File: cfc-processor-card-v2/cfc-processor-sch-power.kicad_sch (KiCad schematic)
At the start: 88 parts, among them Q1 DMP2240UDM, Q2 PMV45EN, Q3 DMP3050LVT-7, Q4 DMP3050LVT-7, Q5 PMV45EN, U1 MAX7310ATE+, U2 MIC842LYC5, U3 MIC842LYC5, U4 TS5A21366, U5 MAX4211FETE, U6 TPS62112

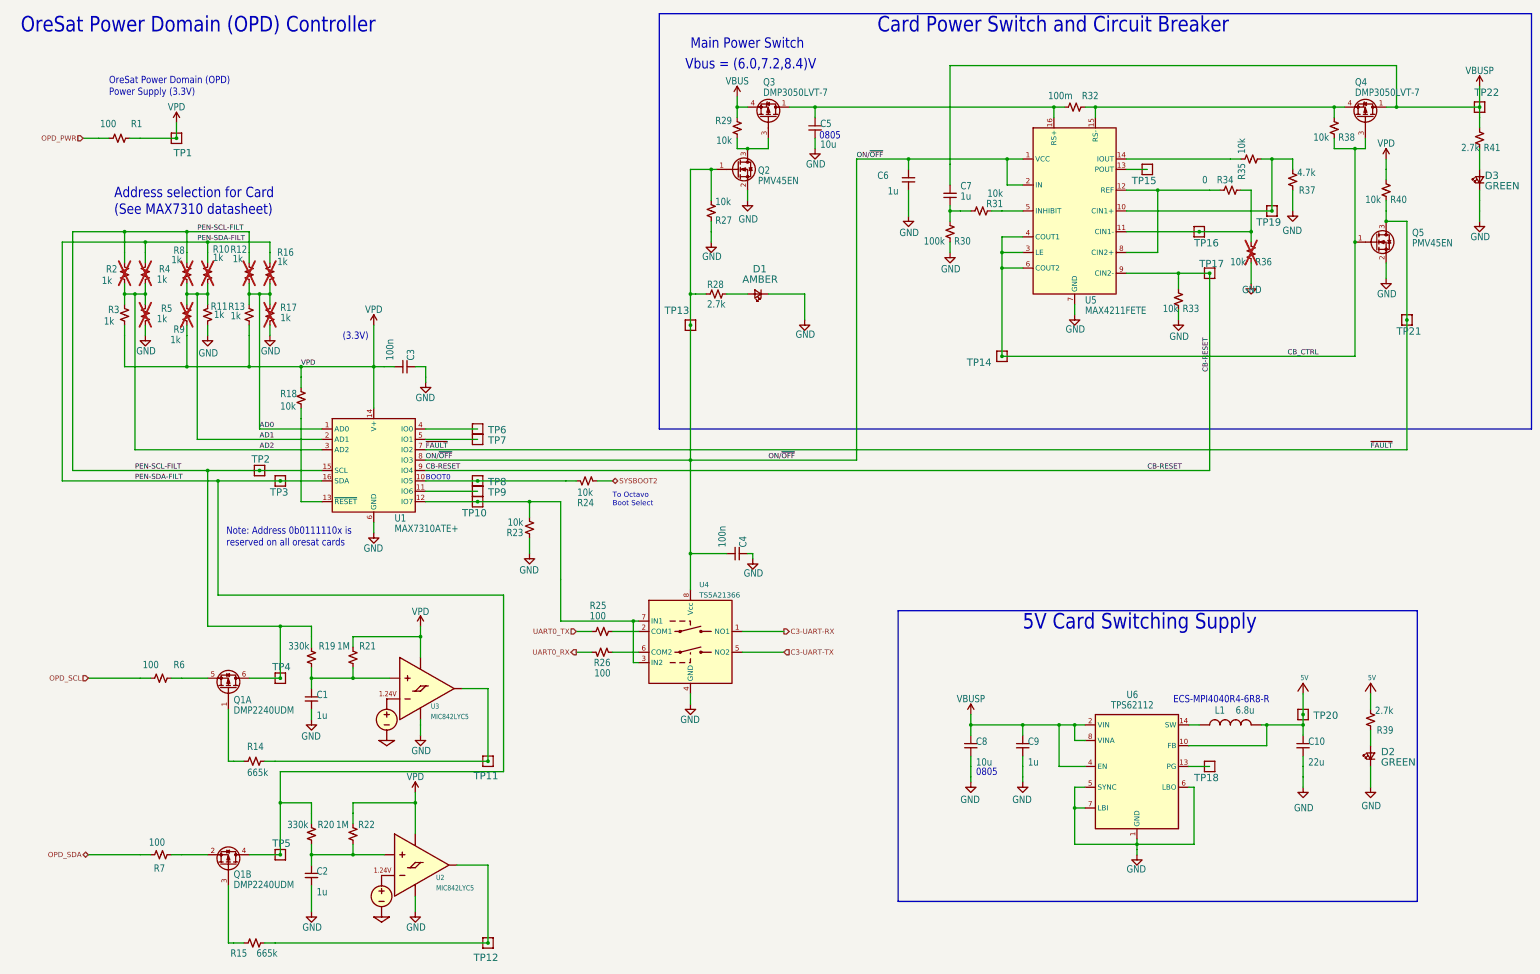
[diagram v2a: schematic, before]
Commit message: Updated OPD
couple of resistors and caps added to schematic. Changed USB ESD clamp VDD to 3.3v instead of octavo created VDD line.
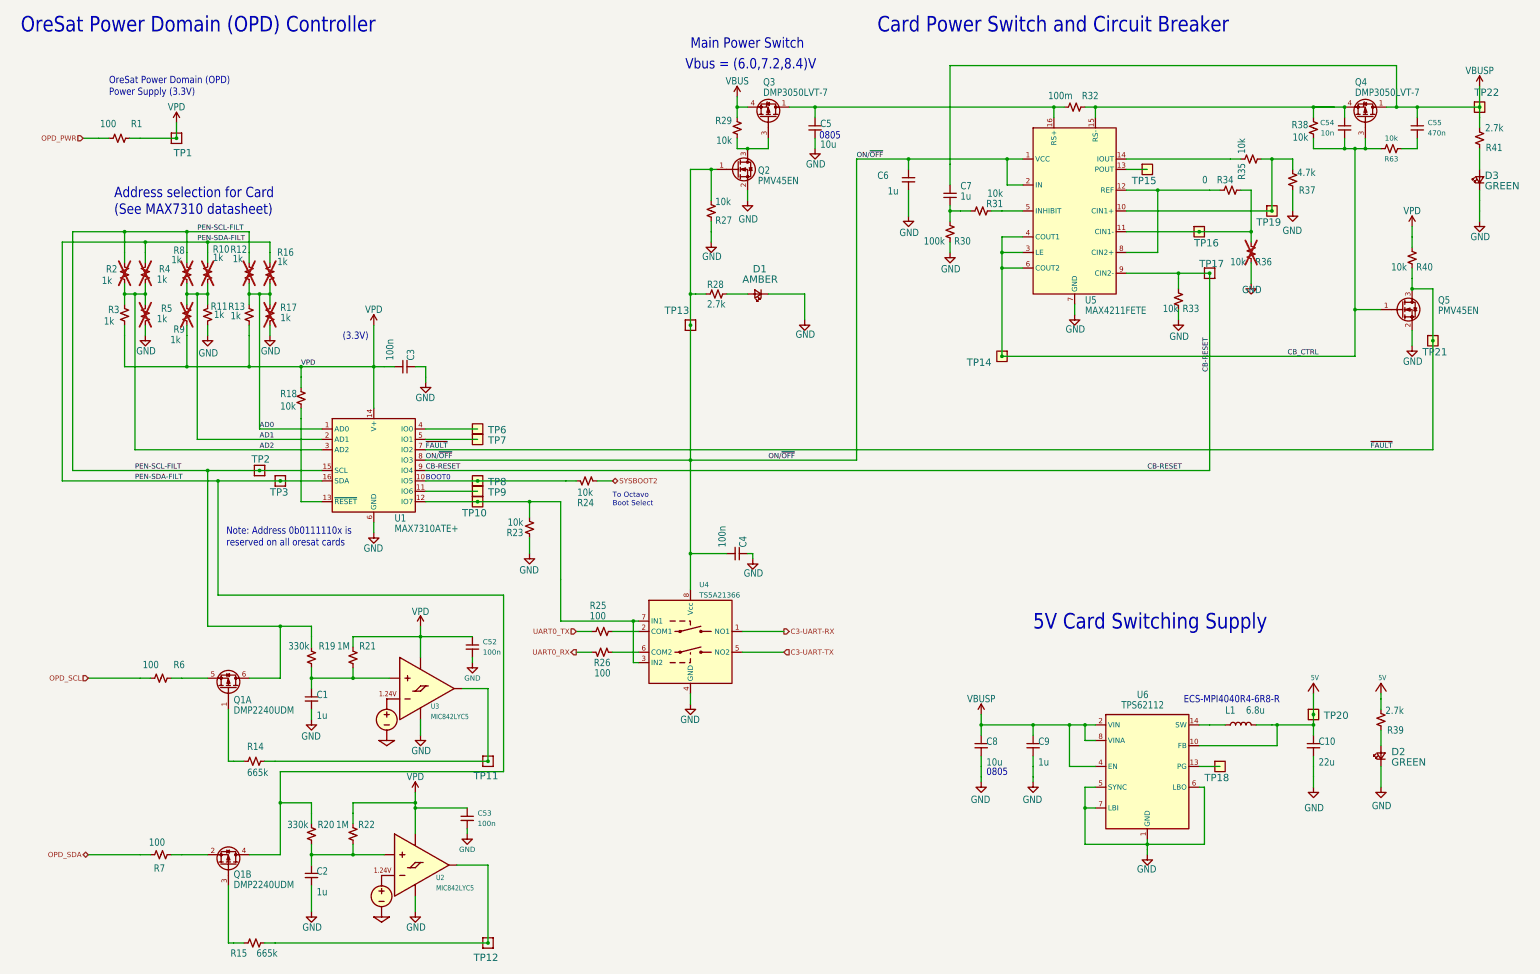
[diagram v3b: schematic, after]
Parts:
- removed TP4, TP5: TEST-POINT, cfc-card:2MM-TEST-POINT, symbol cfc-card-eagle-import:TEST-POINT
- added C52, C53: 100n, oresat-passives:0603-C-NOSILK, symbol Device:C_Small
- added C54: 10n, oresat-passives:0603-C-NOSILK, symbol Device:C_Small
- added C55: 470n, oresat-passives:0603-C-NOSILK, symbol Device:C_Small
- added R63: 10k, oresat-passives:0603-C-NOSILK, symbol Device:R_Small_US
- L1: symbol cfc-card-eagle-import:L-ECS-MPI4040 -> Device:L
- TP10, TP14, TP15, TP16, TP18, TP19, TP20, TP21, TP22, TP6, TP7, TP8, TP9: footprint cfc-card:2MM-TEST-POINT -> oresat-misc:TestPoint-0.75mm-th; symbol cfc-card-eagle-import:TEST-POINT -> Oresat Misc:Test-Point-0.75mm-th
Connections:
- net CB_CTRL: now also C54.2, R63.2
- net GND: now also C52.2, C53.2
- net VBUSP: now also C55.1
- net VPD: now also C52.1, C53.1
- net at Q4.4 (S), R32.2, R38.2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: now also C54.1
- new net: C55.2, R63.1
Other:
- moved on the sheet: C10, C8, C9, D2, Q5, R38, R39, R40, U6

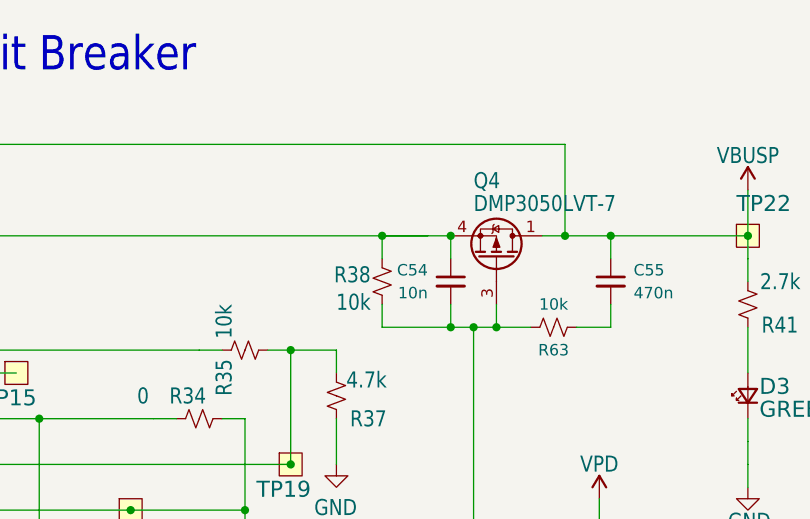
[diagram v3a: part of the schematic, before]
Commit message: Update
Added pull down resistors and removed therm + and sensor enable and added i2c support for cfc sensor card.
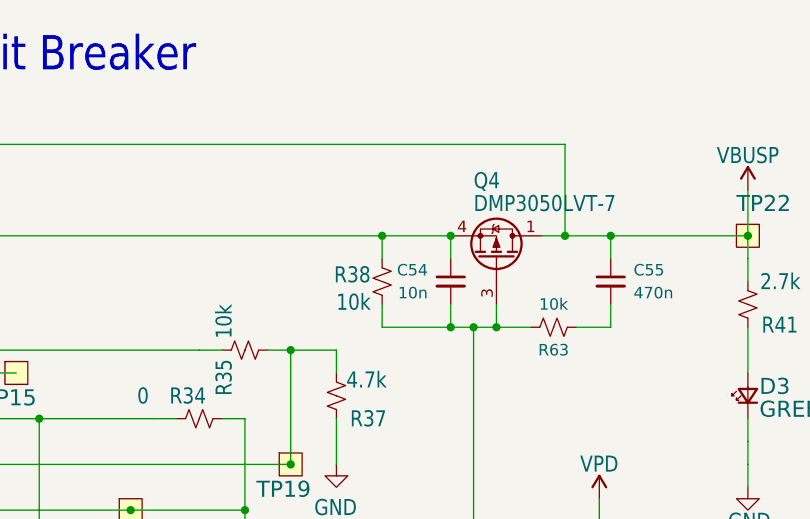
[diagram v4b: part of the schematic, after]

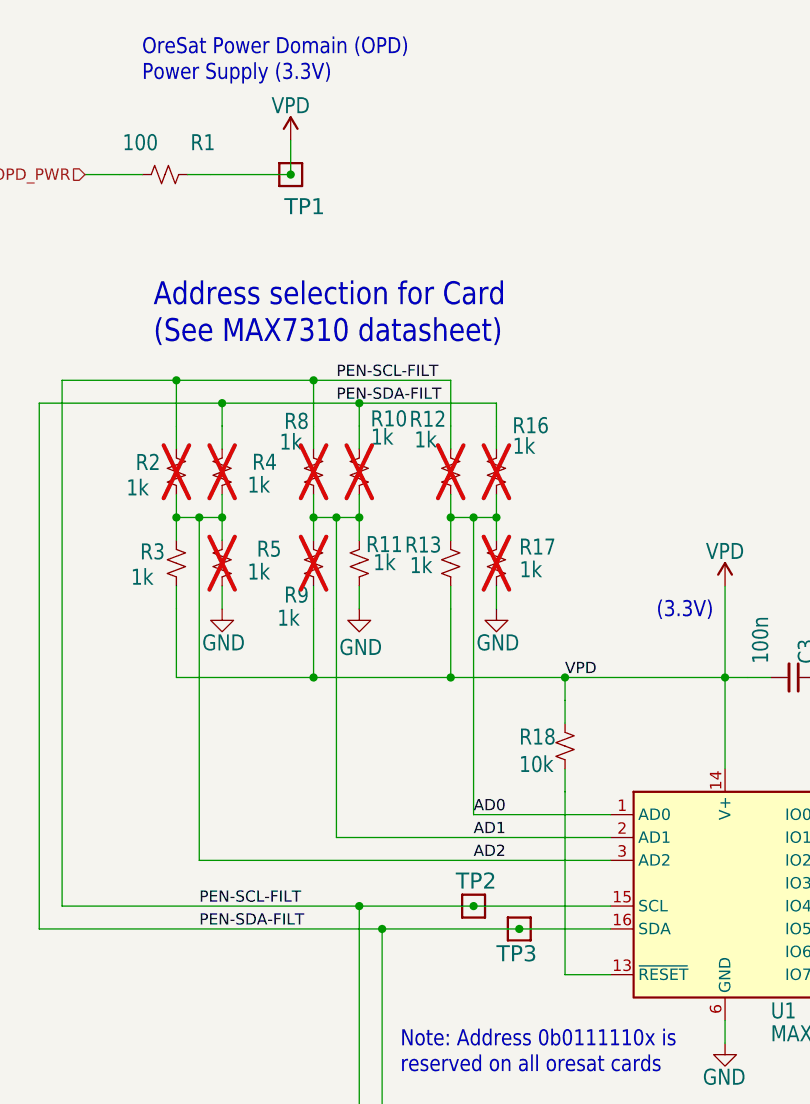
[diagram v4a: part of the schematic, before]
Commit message: Update
Fixed a couple of library issues on testpoints and other misc components. Added Pull up resistors to 8 channel i2c ic
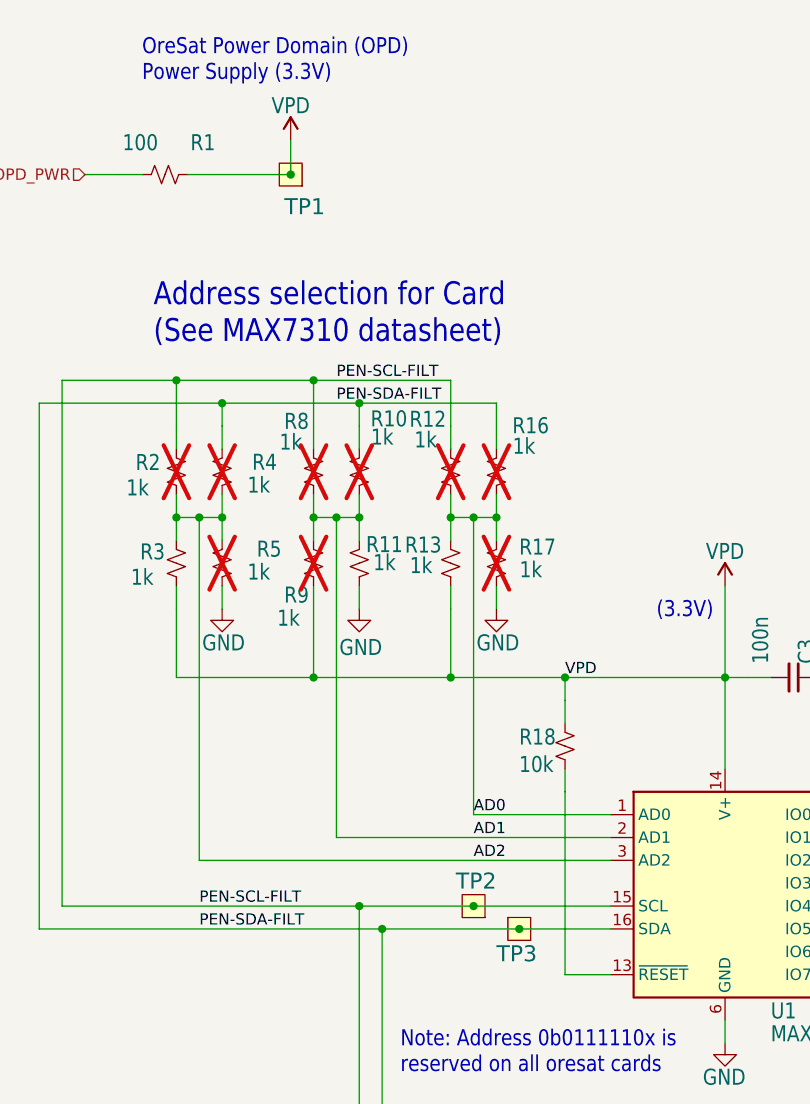
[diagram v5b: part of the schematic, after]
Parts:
- TP1, TP2, TP3: footprint cfc-card:2MM-TEST-POINT -> oresat-misc:TestPoint-0.75mm-th; symbol cfc-card-eagle-import:TEST-POINT -> oresat-misc:Test-Point-0.75mm-th
- TP10, TP14, TP15, TP16, TP18, TP19, TP20, TP21, TP22, TP6, TP7, TP8, TP9: symbol Oresat Misc:Test-Point-0.75mm-th -> oresat-misc:Test-Point-0.75mm-th
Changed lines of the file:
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@@
 	)
 	(symbol
-		(lib_id "cfc-card-eagle-import:TEST-POINT")
+		(lib_id "oresat-misc:Test-Point-0.75mm-th")
 		(at 105.41 132.08 0)
 		(unit 1)
@@
 			)
 		)
-		(property "Footprint" "cfc-card:2MM-TEST-POINT"
-			(at 105.41 132.08 0)
+		(property "Footprint" "oresat-misc:TestPoint-0.75mm-th"
+			(at 105.41 121.92 0)
 			(hide yes)
 			(show_name no)
@@
 			)
 		)
-		(property "Description" ""
+		(property "Description" "0.75 mm TH test point; good for scope probes and jumpers"
 			(at 105.41 132.08 0)
 			(hide yes)
@@
 	)
 	(symbol
-		(lib_id "Oresat Misc:Test-Point-0.75mm-th")
+		(lib_id "oresat-misc:Test-Point-0.75mm-th")
 		(at 335.28 201.93 0)
 		(unit 1)
@@
 	)
 	(symbol
-		(lib_id "Oresat Misc:Test-Point-0.75mm-th")
+		(lib_id "oresat-misc:Test-Point-0.75mm-th")
 		(at 358.14 189.23 0)
 		(unit 1)
@@
 	)
 	(symbol
-		(lib_id "Oresat Misc:Test-Point-0.75mm-th")
+		(lib_id "oresat-misc:Test-Point-0.75mm-th")
 		(at 153.67 137.16 0)
 		(unit 1)
@@
 	)
 	(symbol
-		(lib_id "Oresat Misc:Test-Point-0.75mm-th")
+		(lib_id "oresat-misc:Test-Point-0.75mm-th")
 		(at 398.78 40.64 0)
 		(unit 1)
@@
 	)
 	(symbol
-		(lib_id "Oresat Misc:Test-Point-0.75mm-th")
+		(lib_id "oresat-misc:Test-Point-0.75mm-th")
 		(at 347.98 66.04 0)
 		(unit 1)
@@
 	)
 	(symbol
-		(lib_id "Oresat Misc:Test-Point-0.75mm-th")
+		(lib_id "oresat-misc:Test-Point-0.75mm-th")
 		(at 153.67 132.08 90)
 		(unit 1)
@@
 	)
 	(symbol
-		(lib_id "Oresat Misc:Test-Point-0.75mm-th")
+		(lib_id "oresat-misc:Test-Point-0.75mm-th")
 		(at 330.2 71.12 0)
 		(unit 1)
@@
 	)
 	(symbol
-		(lib_id "Oresat Misc:Test-Point-0.75mm-th")
+		(lib_id "oresat-misc:Test-Point-0.75mm-th")
 		(at 317.5 55.88 0)
 		(unit 1)
@@
 	)
 	(symbol
-		(lib_id "Oresat Misc:Test-Point-0.75mm-th")
+		(lib_id "oresat-misc:Test-Point-0.75mm-th")
 		(at 387.35 97.79 0)
 		(unit 1)
@@
 	)
 	(symbol
-		(lib_id "Oresat Misc:Test-Point-0.75mm-th")
+		(lib_id "oresat-misc:Test-Point-0.75mm-th")
 		(at 153.67 121.92 90)
 		(unit 1)
@@
 	)
 	(symbol
-		(lib_id "cfc-card-eagle-import:TEST-POINT")
+		(lib_id "oresat-misc:Test-Point-0.75mm-th")
 		(at 80.01 48.26 180)
 		(unit 1)
@@
 			)
 		)
-		(property "Footprint" "cfc-card:2MM-TEST-POINT"
-			(at 80.01 48.26 0)
+		(property "Footprint" "oresat-misc:TestPoint-0.75mm-th"
+			(at 80.01 58.42 0)
 			(hide yes)
 			(show_name no)
@@
 			)
 		)
-		(property "Description" ""
+		(property "Description" "0.75 mm TH test point; good for scope probes and jumpers"
 			(at 80.01 48.26 0)
 			(hide yes)
@@
 	)
 	(symbol
-		(lib_id "Oresat Misc:Test-Point-0.75mm-th")
+		(lib_id "oresat-misc:Test-Point-0.75mm-th")
 		(at 281.94 101.6 0)
 		(mirror y)
@@
 	)
 	(symbol
-		(lib_id "Oresat Misc:Test-Point-0.75mm-th")
+		(lib_id "oresat-misc:Test-Point-0.75mm-th")
 		(at 153.67 134.62 90)
 		(unit 1)
@@
 	)
 	(symbol
-		(lib_id "Oresat Misc:Test-Point-0.75mm-th")
+		(lib_id "oresat-misc:Test-Point-0.75mm-th")
 		(at 153.67 119.38 90)
 		(unit 1)
@@
 	)
 	(symbol
-		(lib_id "cfc-card-eagle-import:TEST-POINT")
+		(lib_id "oresat-misc:Test-Point-0.75mm-th")
 		(at 100.33 129.54 180)
 		(unit 1)
@@
 			)
 		)
-		(property "Footprint" "cfc-card:2MM-TEST-POINT"
-			(at 100.33 129.54 0)
+		(property "Footprint" "oresat-misc:TestPoint-0.75mm-th"
+			(at 100.33 139.7 0)
 			(hide yes)
 			(show_name no)
@@
 			)
 		)
-		(property "Description" ""
+		(property "Description" "0.75 mm TH test point; good for scope probes and jumpers"
 			(at 100.33 129.54 0)
 			(hide yes)
